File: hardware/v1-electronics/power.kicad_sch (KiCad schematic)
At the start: 40 parts, among them IC3 BQ25186DLHR, IC4 TPS61288LRQQR, IC5 MP2721GRH-0000-Z, J1 USB_C_Receptacle_USB2.0_14P, J3 Conn_01x02, J4 Conn_01x02, SW77 SW_Push, SW78 SW_Push, U2 TPS613222ADBZ

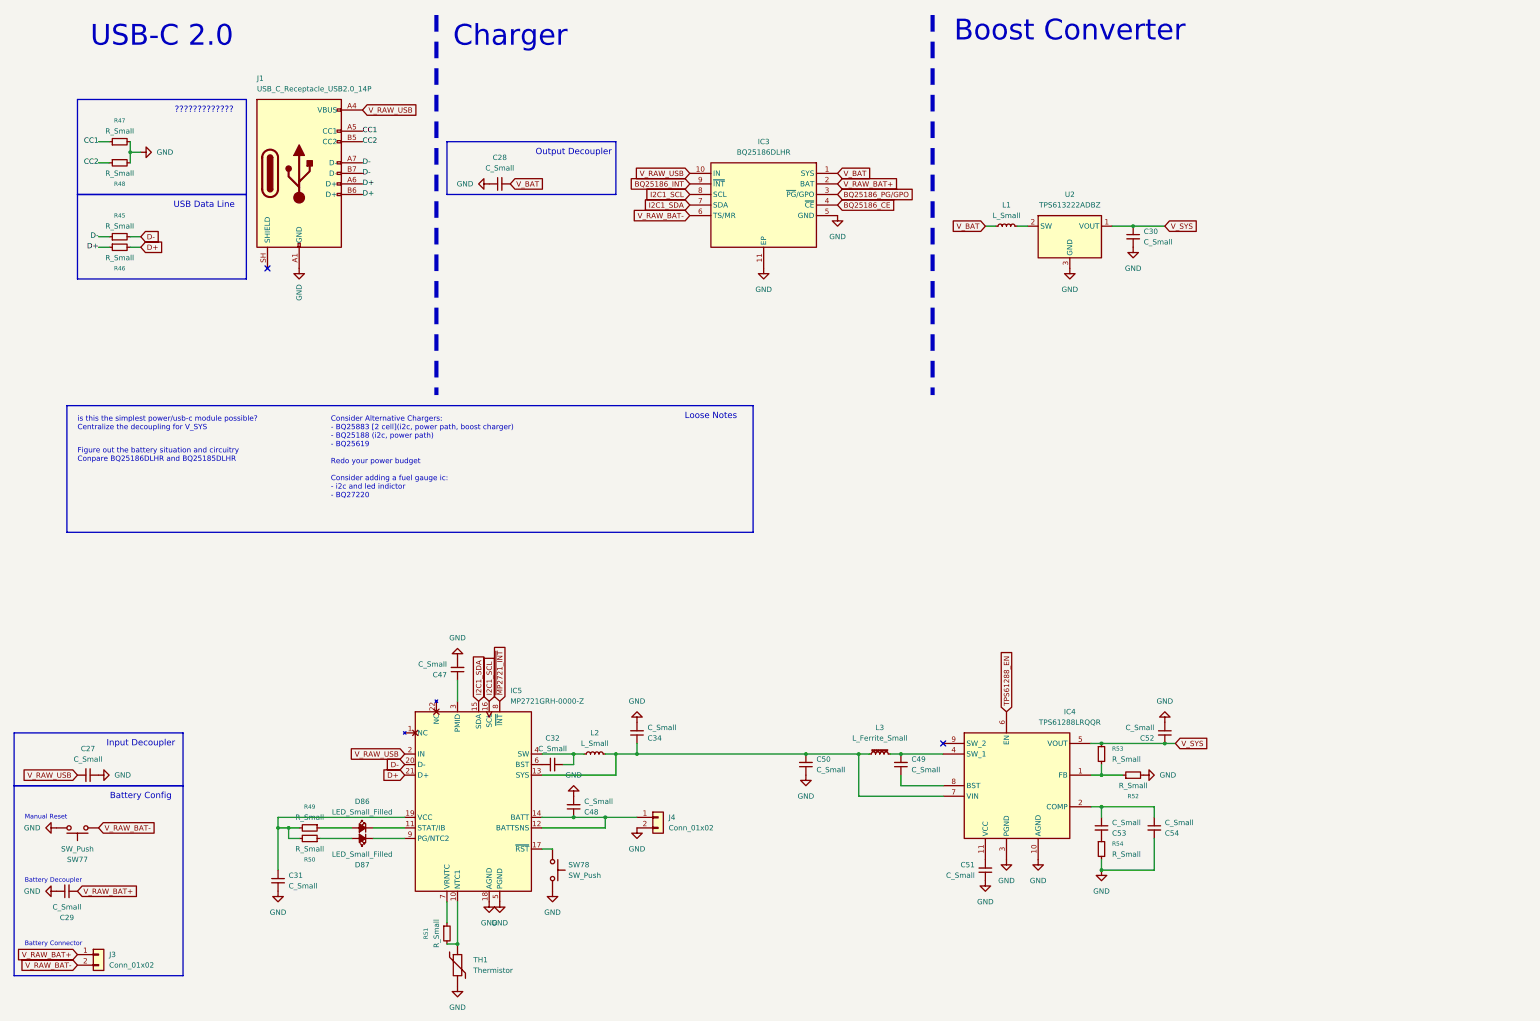
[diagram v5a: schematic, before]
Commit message: refactor(v1 hardware): power train part 2
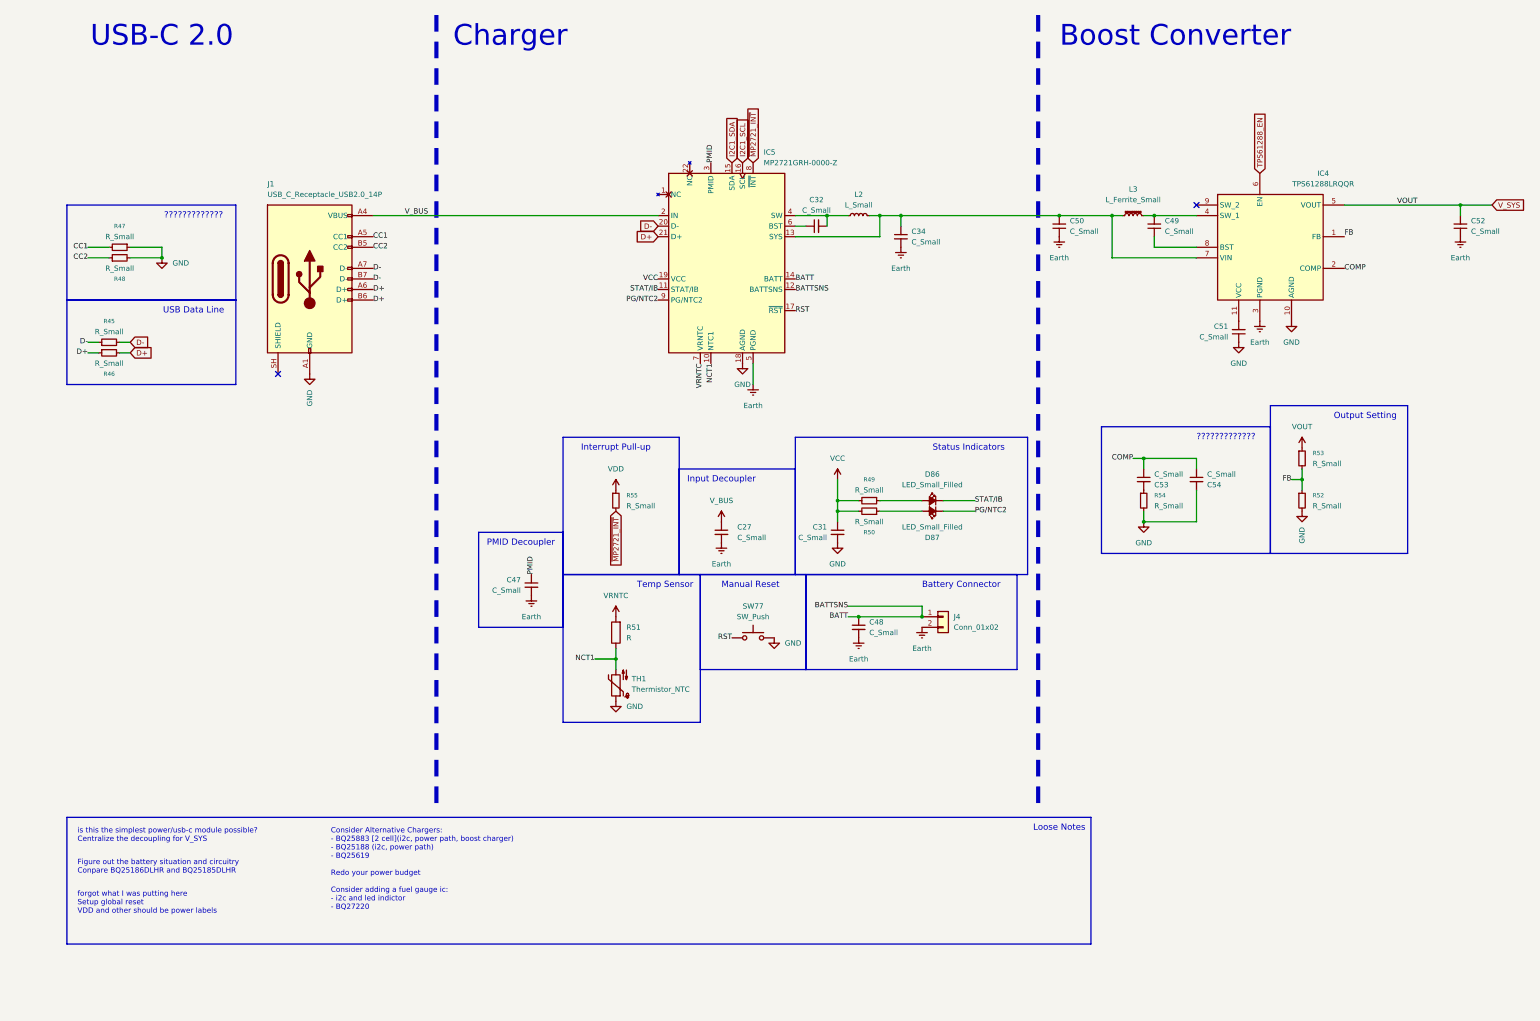
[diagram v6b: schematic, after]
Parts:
- removed C28, C29, C30: C_Small, symbol Device:C_Small
- removed IC3: BQ25186DLHR, Texas Instruments:SON40P220X200X80-11N, symbol Texas Instruments:BQ25186DLHR
- removed J3: Conn_01x02, symbol Connector_Generic:Conn_01x02
- removed L1: L_Small, symbol Device:L_Small
- removed R51: R_Small, symbol Device:R_Small
- removed SW78: SW_Push, symbol Switch:SW_Push
- removed TH1: Thermistor, symbol Device:Thermistor
- removed U2: TPS613222ADBZ, Package_TO_SOT_SMD:SOT-23, symbol Regulator_Switching:TPS613222ADBZ
- added R51: R, symbol Device:R
- added R55: R_Small, symbol Device:R_Small
- added TH1: Thermistor_NTC, symbol Device:Thermistor_NTC
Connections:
- net V_RAW_BAT- is gone; now on net RST: SW77.2
- net CC1: now also R47.2; no longer R47.1
- net GND: now also R47.1, TH1.1; no longer C27.1, C34.2, C47.2, C48.2, C50.1, C52.1, IC4.3 (PGND), IC5.5 (PGND), J4.2 (Pin_2), R47.2
- net ~{MP2721_INT}: now also R55.2
- net VCC: now reaches C31.1, IC5.19 (VCC), R49.2, R50.2
- net NCT1: now reaches IC5.10 (NTC1)
- net NCT1: now also R51.1, TH1.2
- net PG/NTC2: now reaches D87.1 (K), IC5.9 (PG/NTC2)
- net STAT/IB: now reaches D86.1 (K), IC5.11 (STAT/IB)
- net COMP: now reaches C53.1, C54.1, IC4.2 (COMP)
- net PMID: now reaches C47.1, IC5.3 (PMID)
- net FB: now reaches IC4.1 (FB), R52.1, R53.2
- net BATT: now reaches C48.1, IC5.12 (BATTSNS), IC5.14 (BATT), J4.1 (Pin_1)
- net RST: now reaches IC5.17 (~{RST})
- net VRNTC: now reaches IC5.7 (VRNTC)
- net VRNTC: now also R51.2
- net V_RAW_USB renamed V_BUS
- net V_BUS: now also C27.1; no longer C27.2
- net V_SYS renamed VOUT
- new net Earth: C27.2, C34.2, C47.2, C48.2, C50.1, C52.1, IC4.3 (PGND), IC5.5 (PGND), J4.2 (Pin_2)
- new net VDD: R55.1
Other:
- note added: "Interrupt Pull-up"
- note added: "Output Setting"
- note added: "PMID Decoupler"
- note added: "Status Indicators"
- note added: "Temp Sensor"
- note added: "forgot what I was putting here Setup global reset VDD and other should be power labels"
- note removed: "Battery Config"
- note removed: "Battery Decoupler"
- note removed: "Output Decoupler"
- moved on the sheet: C27, C32, C34, C49, C50, C51, C52, IC4, IC5, J1, L2, L3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

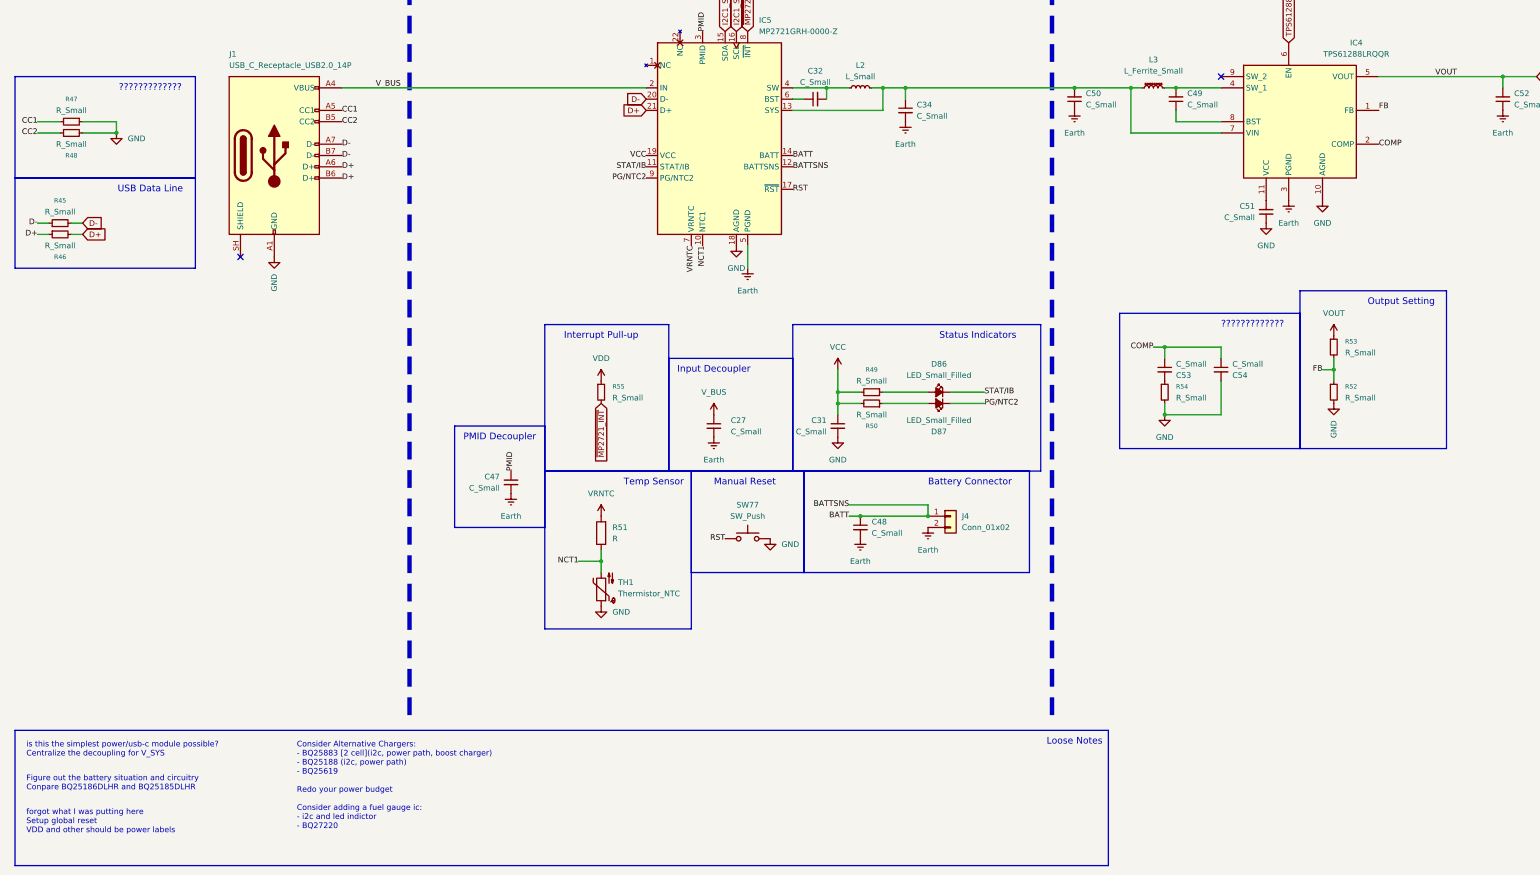
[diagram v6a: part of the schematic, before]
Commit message: refactor(v1 hardware): power system refactor complete
- changed components and cleaned up schematic
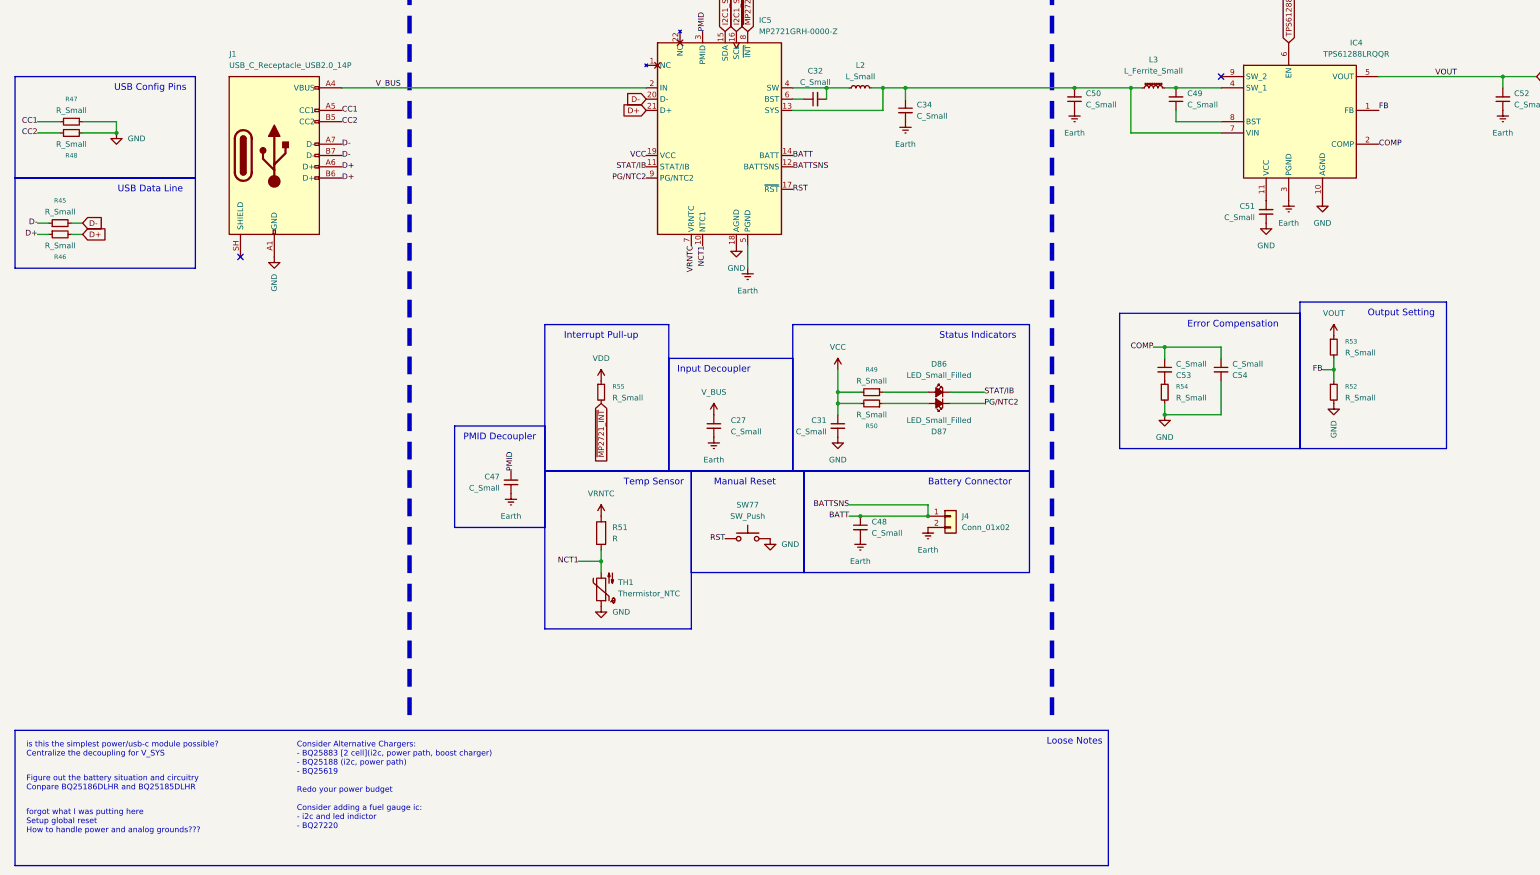
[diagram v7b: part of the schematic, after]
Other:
- note added: "Error Compensation"
- note added: "USB Config Pins"
- note added: "forgot what I was putting here Setup global reset How to handle power and analog grounds???"
- note removed: "?????????????"
- note removed: "forgot what I was putting here Setup global reset VDD and other should be power labels"
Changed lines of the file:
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@@
 	)
 	(rectangle
-		(start 302.26 106.68)
+		(start 302.26 109.22)
 		(end 335.28 142.24)
 		(stroke
@@
 	(rectangle
 		(start 187.96 114.3)
-		(end 243.84 147.32)
+		(end 241.3 147.32)
 		(stroke
 			(width 0.2)
@@
 		)
 	)
-	(text "?????????????"
-		(exclude_from_sim no)
-		(at 284.48 114.3 0)
+	(text "Error Compensation"
+		(exclude_from_sim no)
+		(at 276.86 114.3 0)
 		(effects
 			(font
@@
 	(text "Output Setting"
 		(exclude_from_sim no)
-		(at 317.5 109.22 0)
+		(at 317.5 111.76 0)
 		(effects
 			(font
@@
 		)
 	)
-	(text "?????????????"
+	(text "USB Config Pins"
 		(exclude_from_sim no)
 		(at 43.18 60.96 0)
@@
 		)
 	)
-	(text "forgot what I was putting here\nSetup global reset\nVDD and other should be power labels"
+	(text "forgot what I was putting here\nSetup global reset\nHow to handle power and analog grounds???"
 		(exclude_from_sim no)
 		(at 15.24 223.52 0)
@@
 		)
 		(stroke
-			(width 0)
+			(width 0.5)
 			(type default)
 		)
@@
 		)
 		(stroke
-			(width 0)
+			(width 0.5)
 			(type default)
 		)
@@
 		)
 		(stroke
-			(width 0)
+			(width 0.5)
 			(type default)
 		)
@@
 		)
 		(stroke
-			(width 0)
+			(width 0.5)
 			(type default)
 		)
@@
 		)
 		(stroke
-			(width 0)
+			(width 0.5)
 			(type default)
 		)
@@
 		)
 		(stroke
-			(width 0)
+			(width 0.5)
 			(type default)
 		)
@@
 		)
 		(stroke
-			(width 0)
+			(width 0.5)
 			(type default)
 		)
@@
 		)
 		(stroke
-			(width 0)
+			(width 0.5)
 			(type default)
 		)
@@
 		)
 		(stroke
-			(width 0)
+			(width 0.5)
 			(type default)
 		)
@@
 		)
 		(stroke
-			(width 0)
-			(type default)
-		)
+			(width 0.5)
+			(type default)
+		)

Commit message: feat(v1 hardware): add protection to usb-c port
added ESD protection and EMI filtering
start assigning values to passive components
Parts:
- removed C32: C_Small, symbol Device:C_Small
- removed L2: L_Small, symbol Device:L_Small
- removed R45, R46: R_Small, symbol Device:R_Small
- added C46: 22nF, symbol Device:C_Small
- added FL1: EXC14CE900U, EXC14CE900U, symbol Panasonic:EXC14CE900U
- added IC3: USBLC6-2SC6, SOT95P280X145-6N, symbol STMicroelectronics:USBLC6-2SC6
- added L4: L_Small, symbol Device:L_Small
- C27, C47: value C_Small -> 1uF
- C31: value C_Small -> 4.7uF
- C34, C48: value C_Small -> 20uF
- R47, R48: value R_Small -> 5.1k
- R49, R50, R55: value R_Small -> 10k
- R51: value R -> 10k
- TH1: value Thermistor_NTC -> MF52A103J3435
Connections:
- net D+: now also FL1.4; no longer J1.A6 (D+), J1.B6 (D+)
- net D-: now also FL1.3; no longer J1.A7 (D-), J1.B7 (D-)
- net GND: now also J1.SH (SHIELD), IC3.2 (GND)
- net V_BUS: now also IC3.5 (VBUS)
- net SW: now reaches IC5.4 (SW)
- net SW: now also C46.1, L4.2
- net BST: now reaches IC5.6 (BST)
- net BST: now also C46.2
- new net: FL1.2, IC3.1 (I/O1), IC3.6 (I/O1), J1.A7 (D-), J1.B7 (D-)
- new net: FL1.1, IC3.3 (I/O2), IC3.4 (I/O2), J1.A6 (D+), J1.B6 (D+)
- new net V_CHRG: L4.1
- no-connect marks 2 -> 1
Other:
- note added: "Data Line EMI Filter"
- note added: "Data Line ESD Protection"
- note added: "Regulator Config"
- note removed: "USB Data Line"
- moved on the sheet: C27, C31, C34, C47, C48, C49, C50, C51, C52, C53, C54, D86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
